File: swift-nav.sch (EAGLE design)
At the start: 167 parts, among them J1 SMA_EDGE, J6 ZX62-B-5PA, U1 6SLX9FTG256, U10 MAX2769, U12 PT7M8206B33TA5EX, U13 M25PX80, U2 LTC3407A_DFN, U3 STM32-M-64-LQFP, U4 7Q-16.368MBG-T, U5 SMA_PATCH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

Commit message: VUSB pulldown + other shiz
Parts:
- added R8: 10K, pel_dipol_comp:RESISTOR-0402
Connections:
- net GND: now also R8.1
- net V_USB: now also R8.2
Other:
- moved on the sheet: D1
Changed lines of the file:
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@@
 <part name="H3" library="swift-nav" deviceset="MOUNT-PAD-ROUND" device="M3"/>
 <part name="H4" library="swift-nav" deviceset="MOUNT-PAD-ROUND" device="M3"/>
+<part name="R8" library="pel_dipol_comp" deviceset="RESISTOR" device="-0402" value="10K"/>
+<part name="GND79" library="supply1" deviceset="GND" device=""/>
 </parts>
 <sheets>
@@
 <instance part="LED1" gate="G$1" x="162.56" y="243.84"/>
 <instance part="LED2" gate="G$1" x="172.72" y="243.84"/>
-<instance part="P+7" gate="1" x="71.12" y="218.44" smashed="yes">
-<attribute name="VALUE" x="69.85" y="219.71" size="1.778" layer="96"/>
+<instance part="P+7" gate="1" x="86.36" y="213.36" smashed="yes">
+<attribute name="VALUE" x="85.09" y="214.63" size="1.778" layer="96"/>
 </instance>
 <instance part="GND2" gate="1" x="347.98" y="286.385"/>
@@
 </instance>
 <instance part="GND73" gate="1" x="377.19" y="63.5"/>
-<instance part="D1" gate="G$1" x="58.42" y="205.74"/>
+<instance part="D1" gate="G$1" x="78.74" y="205.74"/>
 <instance part="X5" gate="G$1" x="36.83" y="138.43" rot="MR180"/>
 <instance part="X6" gate="G$1" x="30.48" y="335.28" rot="R180"/>
@@
 </instance>
 <instance part="GND54" gate="1" x="48.26" y="275.59"/>
+<instance part="R8" gate="G$1" x="71.12" y="200.66" rot="R90"/>
+<instance part="GND79" gate="1" x="71.12" y="193.04"/>
 </instances>
 <busses>
@@
 <pinref part="X1" gate="G$1" pin="1"/>
 </segment>
+<segment>
+<pinref part="R8" gate="G$1" pin="1"/>
+<pinref part="GND79" gate="1" pin="GND"/>
+</segment>
 </net>
 <net name="VCCIO" class="0">
@@
 <segment>
 <pinref part="P+7" gate="1" pin="V+"/>
-<wire x1="71.12" y1="205.74" x2="71.12" y2="215.9" width="0.1524" layer="91"/>
+<wire x1="86.36" y1="205.74" x2="86.36" y2="210.82" width="0.1524" layer="91"/>
 <pinref part="D1" gate="G$1" pin="2"/>
-<wire x1="71.12" y1="205.74" x2="63.5" y2="205.74" width="0.1524" layer="91"/>
+<wire x1="86.36" y1="205.74" x2="83.82" y2="205.74" width="0.1524" layer="91"/>
 </segment>
 <segment>
@@
 <net name="V_USB" class="0">
 <segment>
+<wire x1="327.66" y1="312.42" x2="332.74" y2="312.42" width="0.1524" layer="91"/>
+<pinref part="U3" gate="G$1" pin="PB0-ADC8/TIM3CH3-TIM1CH2N"/>
+<label x="332.74" y="312.42" size="1.778" layer="95"/>
+</segment>
+<segment>
 <wire x1="40.64" y1="200.66" x2="50.8" y2="200.66" width="0.1524" layer="91"/>
 <pinref part="J6" gate="G$1" pin="1"/>
 <wire x1="50.8" y1="200.66" x2="50.8" y2="205.74" width="0.1524" layer="91"/>
+<wire x1="50.8" y1="205.74" x2="71.12" y2="205.74" width="0.1524" layer="91"/>
 <pinref part="D1" gate="G$1" pin="1"/>
-<wire x1="50.8" y1="205.74" x2="53.34" y2="205.74" width="0.1524" layer="91"/>
-<wire x1="50.8" y1="205.74" x2="50.8" y2="215.9" width="0.1524" layer="91"/>
-<junction x="50.8" y="205.74"/>
-<wire x1="50.8" y1="215.9" x2="55.88" y2="215.9" width="0.1524" layer="91"/>
-<label x="55.88" y="215.9" size="1.778" layer="95"/>
-<wire x1="327.66" y1="312.42" x2="332.74" y2="312.42" width="0.1524" layer="91"/>
-<label x="332.74" y="312.42" size="1.778" layer="95"/>
-<pinref part="U3" gate="G$1" pin="PB0-ADC8/TIM3CH3-TIM1CH2N"/>
+<wire x1="71.12" y1="205.74" x2="73.66" y2="205.74" width="0.1524" layer="91"/>
+<pinref part="R8" gate="G$1" pin="2"/>
+<junction x="71.12" y="205.74"/>
+<label x="53.34" y="205.74" size="1.778" layer="95"/>
 </segment>
 </net>

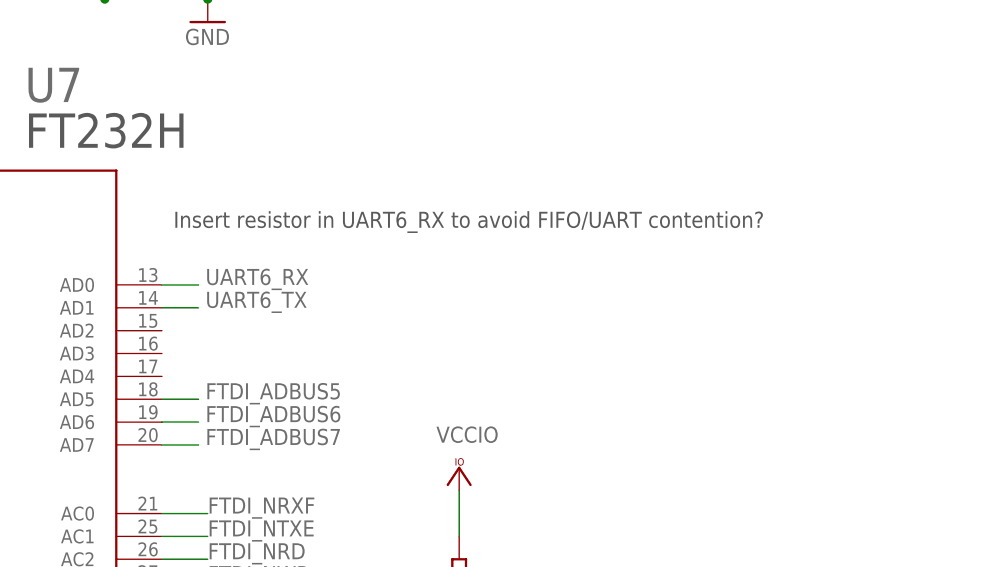
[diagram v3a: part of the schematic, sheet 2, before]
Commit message: UART6 solder jumper for bus contention.
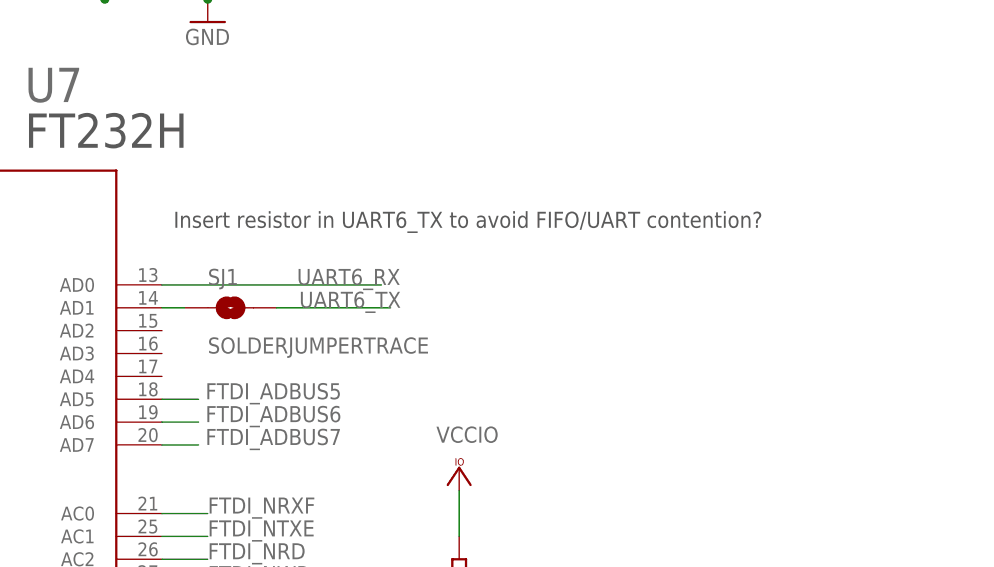
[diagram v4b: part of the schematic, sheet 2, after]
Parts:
- added SJ1: SOLDERJUMPERTRACE, SparkFun-Passives:SOLDERJUMPERTRACE
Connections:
- new net N$2: SJ1.1, U7.AD1
- net UART6_TX: now also SJ1.2; no longer U7.AD1
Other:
- note added: "Insert resistor in UART6_TX to avoid FIFO/UART contention?"
- note removed: "Insert resistor in UART6_RX to avoid FIFO/UART contention?"
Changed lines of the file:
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@@
 <layer number="207" name="207bmp" color="8" fill="10" visible="no" active="yes"/>
 <layer number="208" name="208bmp" color="9" fill="10" visible="no" active="yes"/>
+<layer number="209" name="209bmp" color="7" fill="1" visible="no" active="yes"/>
+<layer number="210" name="210bmp" color="7" fill="1" visible="no" active="yes"/>
+<layer number="211" name="211bmp" color="7" fill="1" visible="no" active="yes"/>
+<layer number="212" name="212bmp" color="7" fill="1" visible="no" active="yes"/>
+<layer number="213" name="213bmp" color="7" fill="1" visible="no" active="yes"/>
+<layer number="214" name="214bmp" color="7" fill="1" visible="no" active="yes"/>
+<layer number="215" name="215bmp" color="7" fill="1" visible="no" active="yes"/>
+<layer number="216" name="216bmp" color="7" fill="1" visible="no" active="yes"/>
+<layer number="217" name="217bmp" color="18" fill="1" visible="no" active="no"/>
+<layer number="218" name="218bmp" color="19" fill="1" visible="no" active="no"/>
+<layer number="219" name="219bmp" color="20" fill="1" visible="no" active="no"/>
+<layer number="220" name="220bmp" color="21" fill="1" visible="no" active="no"/>
+<layer number="221" name="221bmp" color="22" fill="1" visible="no" active="no"/>
+<layer number="222" name="222bmp" color="23" fill="1" visible="no" active="no"/>
+<layer number="223" name="223bmp" color="24" fill="1" visible="no" active="no"/>
+<layer number="224" name="224bmp" color="25" fill="1" visible="no" active="no"/>
 <layer number="231" name="Eagle3D_PG1" color="14" fill="1" visible="yes" active="yes"/>
 <layer number="232" name="Eagle3D_PG2" color="14" fill="2" visible="yes" active="yes"/>
@@
 <part name="R8" library="pel_dipol_comp" deviceset="RESISTOR" device="-0402" value="10K"/>
 <part name="GND79" library="supply1" deviceset="GND" device=""/>
+<part name="SJ1" library="SparkFun-Passives" deviceset="SOLDERJUMPER" device="TRACE"/>
 </parts>
 <sheets>
@@
 <text x="399.415" y="218.44" size="6.4516" layer="94">FT232H UART/FIFO to USB</text>
 <text x="510.54" y="101.6" size="1.778" layer="97">Change to 10k?</text>
-<text x="473.71" y="148.59" size="1.778" layer="97">Insert resistor in UART6_RX to avoid FIFO/UART contention?</text>
+<text x="473.71" y="148.59" size="1.778" layer="97">Insert resistor in UART6_TX to avoid FIFO/UART contention?</text>
 </plain>
 <instances>
@@
 <instance part="R8" gate="G$1" x="71.12" y="200.66" rot="R90"/>
 <instance part="GND79" gate="1" x="71.12" y="193.04"/>
+<instance part="SJ1" gate="1" x="480.06" y="139.7"/>
 </instances>
 <busses>
@@
 <wire x1="215.9" y1="226.06" x2="210.82" y2="226.06" width="0.1524" layer="91"/>
 <label x="198.12" y="226.06" size="1.778" layer="95"/>
-<label x="477.266" y="139.7" size="1.778" layer="95"/>
-<pinref part="U7" gate="G$1" pin="AD1"/>
-<wire x1="476.504" y1="139.7" x2="472.44" y2="139.7" width="0.1524" layer="91"/>
+</segment>
+<segment>
+<pinref part="SJ1" gate="1" pin="2"/>
+<wire x1="485.14" y1="139.7" x2="497.84" y2="139.7" width="0.1524" layer="91"/>
+<label x="487.68" y="139.7" size="1.778" layer="95"/>
 </segment>
 </net>
@@
 <wire x1="215.9" y1="223.52" x2="210.82" y2="223.52" width="0.1524" layer="91"/>
 <label x="198.12" y="223.52" size="1.778" layer="95"/>
-<wire x1="476.504" y1="142.24" x2="472.44" y2="142.24" width="0.1524" layer="91"/>
-<label x="477.266" y="142.24" size="1.778" layer="95"/>
+<wire x1="496.824" y1="142.24" x2="472.44" y2="142.24" width="0.1524" layer="91"/>
+<label x="487.426" y="142.24" size="1.778" layer="95"/>
 <pinref part="U7" gate="G$1" pin="AD0"/>
 </segment>
@@
 </segment>
 </net>
+<net name="N$2" class="0">
+<segment>
+<pinref part="U7" gate="G$1" pin="AD1"/>
+<pinref part="SJ1" gate="1" pin="1"/>
+<wire x1="474.98" y1="139.7" x2="472.44" y2="139.7" width="0.1524" layer="91"/>
+</segment>
+</net>

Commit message: Looots of stuff
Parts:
- removed U$1: LOGO, swift-nav:LOGO
- added C95: 100pF, rcl:C-EUC0402
- added Q1: MOSFET-PCHANNELSMD, SparkFun-DiscreteSemi:MOSFET-PCHANNELSMD
- C15, C16: device rcl:C-EUC0603K -> rcl:C-EUC0402
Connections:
- new net N$18: C2.1, Q1.S, R1.2, U2.MODE/SYNC, U2.RUN/SS1, U2.RUN/SS2, U2.VIN
- new net N$35: C15.2, C16.1, C95.1
- net GND: now also Q1.G
- net N$11: now also C95.2; no longer C15.2, C16.1
- net UART1_RX: now also X6.2; no longer X6.5
- net UART1_TX: now also X6.3; no longer X6.4
- net UART3_RX: now also X1.2; no longer X1.5
- net UART3_TX: now also X1.3; no longer X1.4
- net V+: now also Q1.D, X1.5, X6.5; no longer C2.1, R1.2, U2.MODE/SYNC, U2.RUN/SS1, U2.RUN/SS2, U2.VIN, X1.2, X6.2
- net VCCIO: now also X1.4, X6.4; no longer X1.3, X6.3

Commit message: More stuff
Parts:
- added L3: 250nH/DNP, pel_dipol_comp:INDUCTOR-0402
- L1: value 250nH/DNP -> 250nH
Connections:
- net N$10: now also L3.1
- net N$14: now also L3.2
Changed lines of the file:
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@@
 <setting verticaltext="up"/>
 </settings>
-<grid distance="0.025" unitdist="inch" unit="inch" style="lines" multiple="1" display="yes" altdistance="0.01" altunitdist="inch" altunit="inch"/>
+<grid distance="0.005" unitdist="inch" unit="inch" style="lines" multiple="1" display="yes" altdistance="0.01" altunitdist="inch" altunit="inch"/>
 <layers>
 <layer number="1" name="Top" color="4" fill="1" visible="yes" active="no"/>
@@
 <part name="C12" library="rcl" deviceset="C-EU" device="C0402" value="100pF"/>
 <part name="C13" library="rcl" deviceset="C-EU" device="C0402" value="0.1uF"/>
-<part name="L1" library="pel_dipol_comp" deviceset="INDUCTOR" device="-0402" value="250nH/DNP"/>
+<part name="L1" library="pel_dipol_comp" deviceset="INDUCTOR" device="-0402" value="250nH"/>
 <part name="C14" library="rcl" deviceset="C-EU" device="C0402" value="100pF"/>
 <part name="GND18" library="supply1" deviceset="GND" device=""/>
@@
 <part name="GND80" library="supply1" deviceset="GND" device=""/>
 <part name="C95" library="rcl" deviceset="C-EU" device="C0402" value="100pF"/>
+<part name="L3" library="pel_dipol_comp" deviceset="INDUCTOR" device="-0402" value="250nH/DNP"/>
 </parts>
 <sheets>
@@
 <attribute name="NAME" x="325.374" y="167.386" size="1.778" layer="95" rot="R180"/>
 <attribute name="VALUE" x="338.074" y="167.386" size="1.778" layer="96" rot="R180"/>
+</instance>
+<instance part="L3" gate="G$1" x="286.258" y="154.686" smashed="yes" rot="R180">
+<attribute name="NAME" x="286.258" y="159.131" size="1.778" layer="95" rot="R90"/>
+<attribute name="VALUE" x="292.608" y="154.051" size="1.778" layer="96" rot="R90"/>
 </instance>
 </instances>
@@
 <pinref part="C13" gate="G$1" pin="1"/>
 <pinref part="U10" gate="_ANA" pin="ANT_BIAS"/>
+<pinref part="L3" gate="G$1" pin="1"/>
+<wire x1="305.435" y1="146.05" x2="286.258" y2="146.05" width="0.1524" layer="91"/>
+<wire x1="286.258" y1="146.05" x2="286.258" y2="149.606" width="0.1524" layer="91"/>
+<junction x="305.435" y="146.05"/>
 </segment>
 </net>
@@
 <pinref part="C16" gate="G$1" pin="2"/>
 <pinref part="U5" gate="G$1" pin="1"/>
-<wire x1="289.179" y1="167.132" x2="263.906" y2="167.132" width="0.1524" layer="91"/>
-</segment>
-</net>
+<wire x1="289.179" y1="167.132" x2="286.258" y2="167.132" width="0.1524" layer="91"/>
+<pinref part="L3" gate="G$1" pin="2"/>
+<wire x1="286.258" y1="167.132" x2="263.906" y2="167.132" width="0.1524" layer="91"/>
+<wire x1="286.258" y1="159.766" x2="286.258" y2="167.132" width="0.1524" layer="91"/>
+<junction x="286.258" y="167.132"/>
+</segment>
+</net>

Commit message: Changed FT232 AC7 pullup to V_USB instead of VCCIO Changed RF input from V+ (before PMOS) to VDD (after PMOS) Added pulldown resistor to V_USB
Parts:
- added H5: MOUNT-PAD-ROUNDM3, swift-nav:MOUNT-PAD-ROUNDM3
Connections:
- removed net N$18: C2.1, Q1.S, R1.2, U2.MODE/SYNC, U2.RUN/SS1, U2.RUN/SS2, U2.VIN
- new net VDD: C2.1, C6.2, Q1.S, R1.2, R65.1, U2.MODE/SYNC, U2.RUN/SS1, U2.RUN/SS2, U2.VIN
- net V+: no longer C6.2, R65.1
- net VCCIO: no longer R9.1
- net V_USB: now also R9.1
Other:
- note added: "(1%)"
- note added: "10k?"
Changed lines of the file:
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@@
 <part name="U12" library="jobygnss" deviceset="PT7M8206B33TA5EX" device=""/>
 <part name="P+9" library="supply1" deviceset="V+" device=""/>
-<part name="P+10" library="supply1" deviceset="V+" device=""/>
 <part name="U8" library="jobygnss" deviceset="B4050" device=""/>
 <part name="FRAME3" library="frames" deviceset="FRAME_C_L" device=""/>
@@
 <part name="GND63" library="supply1" deviceset="GND" device=""/>
 <part name="R9" library="pel_dipol_comp" deviceset="RESISTOR" device="-0402" value="39k"/>
-<part name="VCC37" library="supply1" deviceset="VCCIO" device=""/>
 <part name="VCC38" library="supply1" deviceset="VCCIO" device=""/>
 <part name="VCC40" library="supply1" deviceset="VCCIO" device=""/>
@@
 <part name="C95" library="rcl" deviceset="C-EU" device="C0402" value="100pF"/>
 <part name="L3" library="pel_dipol_comp" deviceset="INDUCTOR" device="-0402" value="250nH/DNP"/>
+<part name="H5" library="swift-nav" deviceset="MOUNT-PAD-ROUND" device="M3"/>
+<part name="VDD1" library="supply1" deviceset="VDD" device=""/>
+<part name="VDD2" library="supply1" deviceset="VDD" device=""/>
 </parts>
 <sheets>
@@
 <text x="167.894" y="176.784" size="2.54" layer="97">Spartan Patch Side Optional Bypass - VCCIO</text>
 <text x="167.894" y="150.114" size="2.54" layer="97">Spartan Patch Side Optional Bypass - VCCIO</text>
+<text x="86.36" y="357.124" size="2.54" layer="97">10k?</text>
 </plain>
 <instances>
@@
 <instance part="R65" gate="G$1" x="428.625" y="167.005" smashed="yes">
 <attribute name="NAME" x="424.815" y="168.5036" size="1.778" layer="95"/>
-<attribute name="VALUE" x="429.895" y="168.783" size="1.778" layer="96"/>
+<attribute name="VALUE" x="430.403" y="168.529" size="1.778" layer="96"/>
 </instance>
 <instance part="GND16" gate="1" x="443.865" y="151.765"/>
@@
 </instance>
 <instance part="P+9" gate="1" x="41.275" y="212.725"/>
-<instance part="P+10" gate="1" x="421.005" y="175.895"/>
 <instance part="U8" gate="G$1" x="307.975" y="102.87" rot="R270"/>
 <instance part="C15" gate="G$1" x="304.8" y="162.052" smashed="yes" rot="R180">
@@
 <attribute name="VALUE" x="292.608" y="154.051" size="1.778" layer="96" rot="R90"/>
 </instance>
+<instance part="H5" gate="G$1" x="50.419" y="33.274"/>
+<instance part="VDD1" gate="G$1" x="122.174" y="212.598"/>
+<instance part="VDD2" gate="G$1" x="421.005" y="174.752"/>
 </instances>
 <busses>
@@
 <net name="V+" class="0">
 <segment>
-<wire x1="421.005" y1="167.005" x2="421.005" y2="164.465" width="0.1524" layer="91"/>
-<wire x1="421.005" y1="167.005" x2="423.545" y2="167.005" width="0.1524" layer="91"/>
-<wire x1="421.005" y1="173.355" x2="421.005" y2="167.005" width="0.1524" layer="91"/>
-<junction x="421.005" y="167.005"/>
-<pinref part="C6" gate="G$1" pin="2"/>
-<pinref part="R65" gate="G$1" pin="1"/>
-<pinref part="P+10" gate="1" pin="V+"/>
-</segment>
-<segment>
 <pinref part="P+9" gate="1" pin="V+"/>
 <pinref part="Q1" gate="G$1" pin="D"/>
@@
 </segment>
 </net>
-<net name="N$18" class="0">
+<net name="N$35" class="0">
+<segment>
+<pinref part="C16" gate="G$1" pin="1"/>
+<pinref part="C15" gate="G$1" pin="2"/>
+<wire x1="304.8" y1="167.132" x2="296.799" y2="167.132" width="0.1524" layer="91"/>
+<pinref part="C95" gate="G$1" pin="1"/>
+<wire x1="304.8" y1="167.132" x2="324.993" y2="167.132" width="0.1524" layer="91"/>
+<junction x="304.8" y="167.132"/>
+</segment>
+</net>
+<net name="VDD" class="0">
 <segment>
 <wire x1="76.835" y1="208.915" x2="76.835" y2="205.105" width="0.1524" layer="91"/>
@@
 <wire x1="55.88" y1="208.915" x2="60.96" y2="208.915" width="0.1524" layer="91"/>
 <junction x="60.96" y="208.915"/>
+<wire x1="109.855" y1="208.915" x2="122.174" y2="208.915" width="0.1524" layer="91"/>
+<junction x="109.855" y="208.915"/>
+<pinref part="VDD1" gate="G$1" pin="VDD"/>
+<wire x1="122.174" y1="208.915" x2="122.174" y2="210.058" width="0.1524" layer="91"/>
 </segment>
-</net>
-<net name="N$35" class="0">
 <segment>
-<pinref part="C16" gate="G$1" pin="1"/>
-<pinref part="C15" gate="G$1" pin="2"/>
-<wire x1="304.8" y1="167.132" x2="296.799" y2="167.132" width="0.1524" layer="91"/>
-<pinref part="C95" gate="G$1" pin="1"/>
-<wire x1="304.8" y1="167.132" x2="324.993" y2="167.132" width="0.1524" layer="91"/>
-<junction x="304.8" y="167.132"/>
+<wire x1="421.005" y1="167.005" x2="421.005" y2="164.465" width="0.1524" layer="91"/>
+<wire x1="421.005" y1="167.005" x2="423.545" y2="167.005" width="0.1524" layer="91"/>
+<pinref part="C6" gate="G$1" pin="2"/>
+<pinref part="R65" gate="G$1" pin="1"/>
+<pinref part="VDD2" gate="G$1" pin="VDD"/>
+<wire x1="421.005" y1="172.212" x2="421.005" y2="167.005" width="0.1524" layer="91"/>
+<junction x="421.005" y="167.005"/>
 </segment>
 </net>
@@
 <text x="510.54" y="101.6" size="1.778" layer="97">Change to 10k?</text>
 <text x="473.71" y="148.59" size="1.778" layer="97">Insert resistor in UART6_TX to avoid FIFO/UART contention?</text>
+<text x="403.86" y="73.787" size="1.778" layer="97">(1%)</text>
 </plain>
 <instances>
@@
 </instance>
 <instance part="R7" gate="G$1" x="401.32" y="78.74" smashed="yes" rot="R270">
-<attribute name="VALUE" x="403.86" y="76.962" size="1.778" layer="96"/>
+<attribute name="VALUE" x="403.86" y="76.708" size="1.778" layer="96"/>
 <attribute name="NAME" x="403.86" y="79.502" size="1.778" layer="95"/>
 </instance>
@@
 <attribute name="NAME" x="510.54" y="108.712" size="1.778" layer="95"/>
 </instance>
-<instance part="VCC37" gate="G$1" x="505.46" y="121.92" smashed="yes">
-<attribute name="VALUE" x="502.92" y="124.714" size="1.778" layer="96"/>
-</instance>
 <instance part="VCC38" gate="G$1" x="345.44" y="165.1" smashed="yes">
 <attribute name="VALUE" x="342.9" y="167.894" size="1.778" layer="96"/>
@@
 </segment>
 <segment>
-<pinref part="VCC37" gate="G$1" pin="VCCIO"/>
-<pinref part="R9" gate="G$1" pin="1"/>
-<wire x1="505.46" y1="119.38" x2="505.46" y2="114.3" width="0.1524" layer="91"/>
-</segment>
-<segment>
 <wire x1="345.44" y1="139.7" x2="345.44" y2="162.56" width="0.1524" layer="91"/>
 <pinref part="VCC38" gate="G$1" pin="VCCIO"/>
@@
 <junction x="71.12" y="205.74"/>
 <label x="53.34" y="205.74" size="1.778" layer="95"/>
+<wire x1="505.46" y1="119.634" x2="525.78" y2="119.634" width="0.1524" layer="91"/>
+<pinref part="R9" gate="G$1" pin="1"/>
+<wire x1="505.46" y1="119.634" x2="505.46" y2="114.3" width="0.1524" layer="91"/>
+<label x="525.78" y="119.634" size="2.54" layer="95"/>
 </segment>
 </net>
